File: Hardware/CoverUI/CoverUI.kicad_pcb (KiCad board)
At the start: 2 copper layers, 135 x 88.5 mm, 103 parts, among them J1001 Conn_01x04_Male, J2 Conn_01x06_Male, Q1 BSS138, SW1 SW_MEC_5G, SW10 SW_MEC_5G, SW11 SW_MEC_5G, SW12 SW_MEC_5G, SW13 SW_MEC_5G, SW14 SW_MEC_5G, SW2 SW_MEC_5G, SW3 SW_MEC_5G, SW4 SW_MEC_5G, SW5 SW_MEC_5G, SW6 SW_MEC_5G, SW7 SW_MEC_5G, SW8 SW_MEC_5G, SW9 SW_MEC_5G, U1 Raspberry-Pico, U2 TPIC6C596DRG4, U3 TPIC6C596DRG4, U4 TPIC6C596DRG4, U5 RS0104YQ

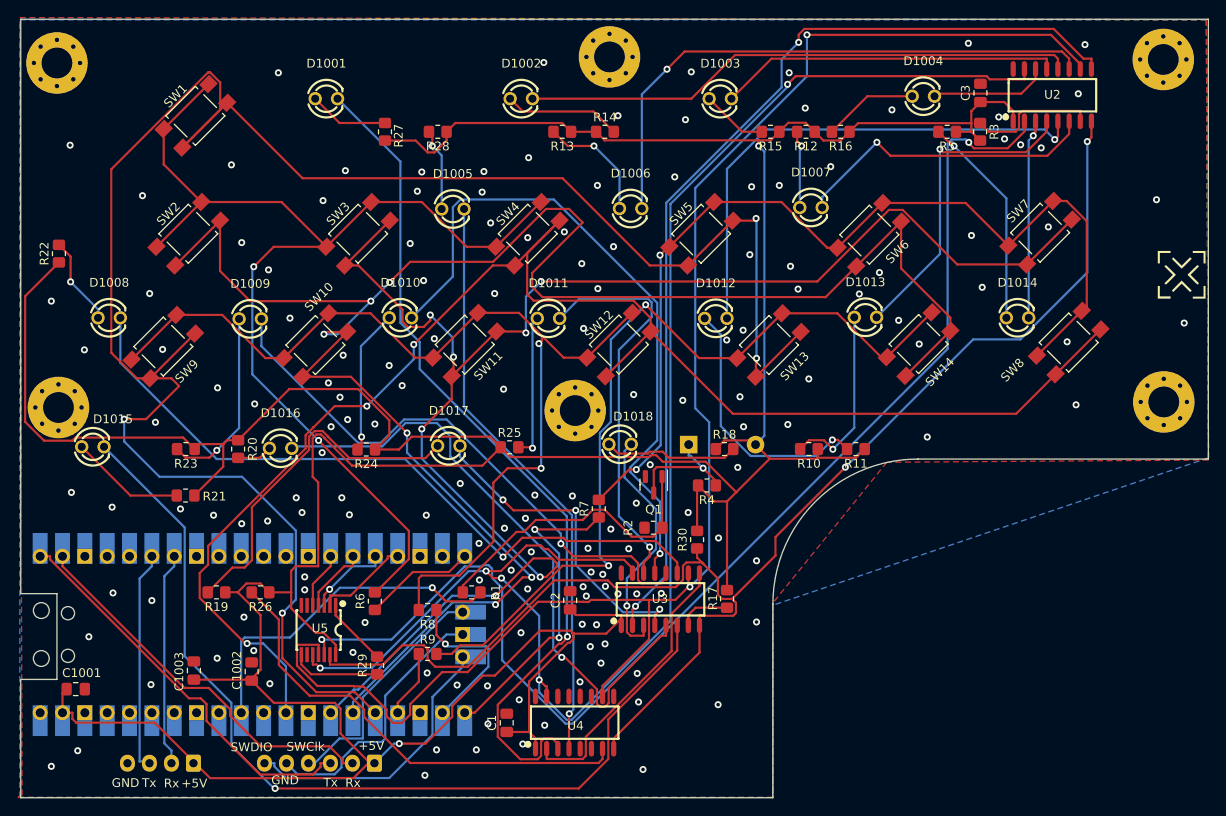
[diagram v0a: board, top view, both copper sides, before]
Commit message: fix(ui): update switch footprints, make central hole smaller
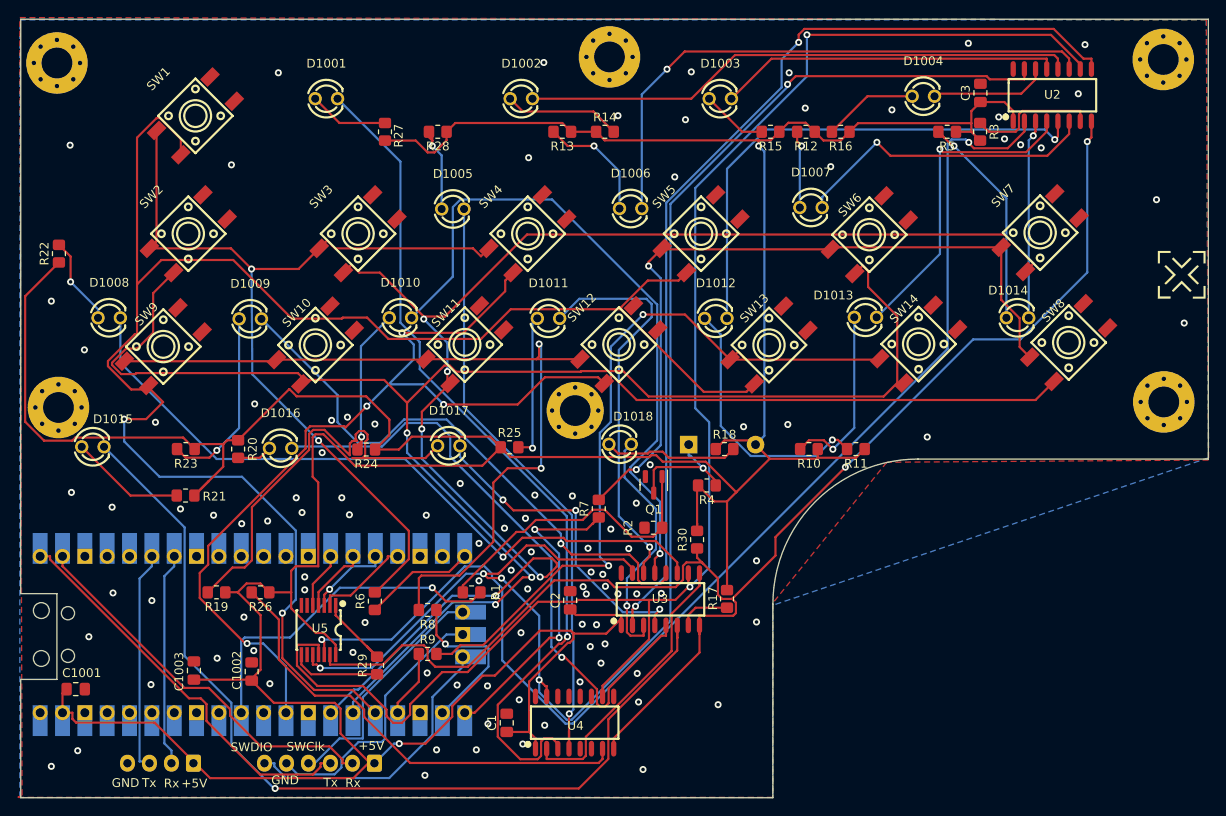
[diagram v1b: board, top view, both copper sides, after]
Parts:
- SW1, SW10, SW11, SW12, SW13, SW14, SW2, SW3, SW4, SW5, SW6, SW7, SW8, SW9: footprint Button_Switch_SMD:SW_SPST_TL3305A -> lcsc:KEY-SMD_4P-L6.0-W6.0-P3.90-LS9.0
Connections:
- SW1 pad 2: /RaspberryPico/GP19 -> (no net)
- SW10 pad 2: /RaspberryPico/GP20 -> (no net)
- SW11 pad 2: /RaspberryPico/GP21 -> (no net)
- SW12 pad 2: /RaspberryPico/GP22 -> (no net)
- SW13 pad 2: /RaspberryPico/GP19 -> (no net)
- SW14 pad 2: /RaspberryPico/GP20 -> (no net)
- SW2 pad 2: /RaspberryPico/GP20 -> (no net)
- SW3 pad 2: /RaspberryPico/GP21 -> (no net)
- SW4 pad 2: /RaspberryPico/GP22 -> (no net)
- SW5 pad 2: /RaspberryPico/GP19 -> (no net)
- SW6 pad 2: /RaspberryPico/GP20 -> (no net)
- SW7 pad 2: /RaspberryPico/GP21 -> (no net)
- SW8 pad 2: /RaspberryPico/GP22 -> (no net)
- SW9 pad 2: /RaspberryPico/GP19 -> (no net)
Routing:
- net /RaspberryPico/GP20: track 219.4 -> 178.9 mm, vias 6 -> 3
- net /RaspberryPico/GP19: track 228.7 -> 193.3 mm, vias 4 -> 2
- net Net-(R6-Pad2): track 126.7 -> 101.5 mm
- net Net-(R7-Pad2): track 109.1 -> 85.2 mm
- net /RaspberryPico/GP21: track 180.7 -> 161.0 mm, vias 7 -> 5
- net Net-(R8-Pad2): track 113.5 -> 94.3 mm
- net /RaspberryPico/GP22: track 174.5 -> 158.4 mm, vias 3 -> 4
- net Net-(R9-Pad2): track 96.6 -> 86.2 mm
- net Net-(D1017-Pad1): track 40.0 -> 48.6 mm
- net Net-(D1005-Pad2): track 66.7 -> 68.7 mm
- net +5V: track 490.6 -> 492.6 mm
- net Net-(D1015-Pad2): track 104.7 -> 106.1 mm
- net Net-(D1005-Pad1): track 8.84 -> 10.00 mm
- net Net-(U3-Pad9): track 31.9 -> 30.8 mm
- net +3.3V: track 7.78 -> 8.82 mm
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
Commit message: fix(ui): connect 3.3V to 3V3
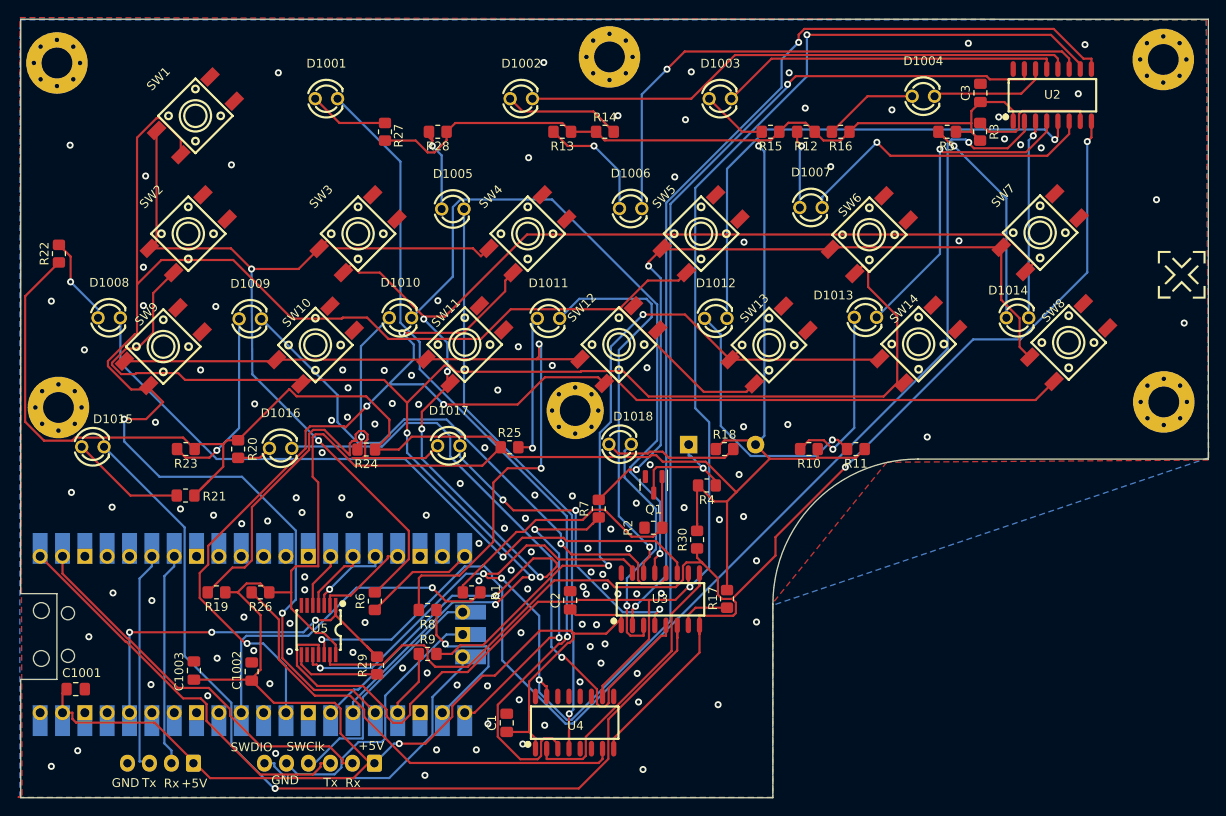
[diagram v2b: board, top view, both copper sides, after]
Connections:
- U1 pad 36: +3V3 -> +3.3V
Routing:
- net +3.3V: track 8.82 -> 43.3 mm, vias 0 -> 3
- net GND: vias 104 -> 132

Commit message: fix(ui): update switches to 4.5mm
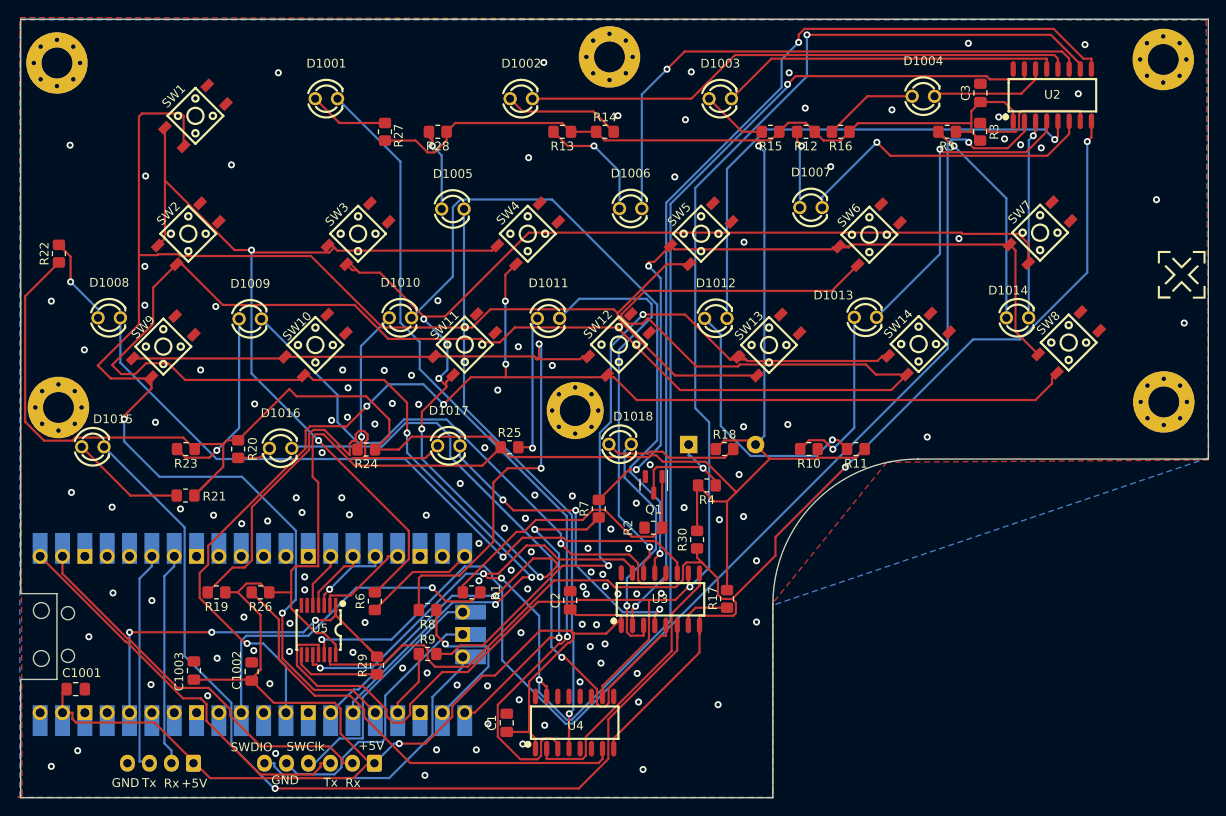
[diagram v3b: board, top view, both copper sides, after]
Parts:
- SW1, SW10, SW11, SW12, SW13, SW14, SW2, SW3, SW4, SW5, SW6, SW7, SW8, SW9: footprint lcsc:KEY-SMD_4P-L6.0-W6.0-P3.90-LS9.0 -> lcsc:SW-SMD_4P-L4.5-W4.5-P3.00-LS7.0
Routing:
- net /RaspberryPico/GP20: track 178.9 -> 260.6 mm
- net /RaspberryPico/GP22: track 158.4 -> 148.3 mm, vias 4 -> 5
- net Net-(R7-Pad2): track 85.2 -> 88.5 mm
- net Net-(R6-Pad2): track 101.5 -> 104.4 mm
- net /RaspberryPico/GP21: track 161.0 -> 163.3 mm
- net /RaspberryPico/GP19: track 193.3 -> 195.0 mm
- net Net-(R9-Pad2): track 86.2 -> 87.6 mm
- net GND: vias 132 -> 131
